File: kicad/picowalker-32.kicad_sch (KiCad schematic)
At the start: 21 parts, among them IC1 TFBS4711-TT1, J1 DBG_HDR, J2 PROGRAM_HDR, SW1 SW_Push, SW2 SW_Push, SW3 SW_Push, U2 M95512-DWDW4TP_K, U3 BMA400, U4 W25Q128JVS

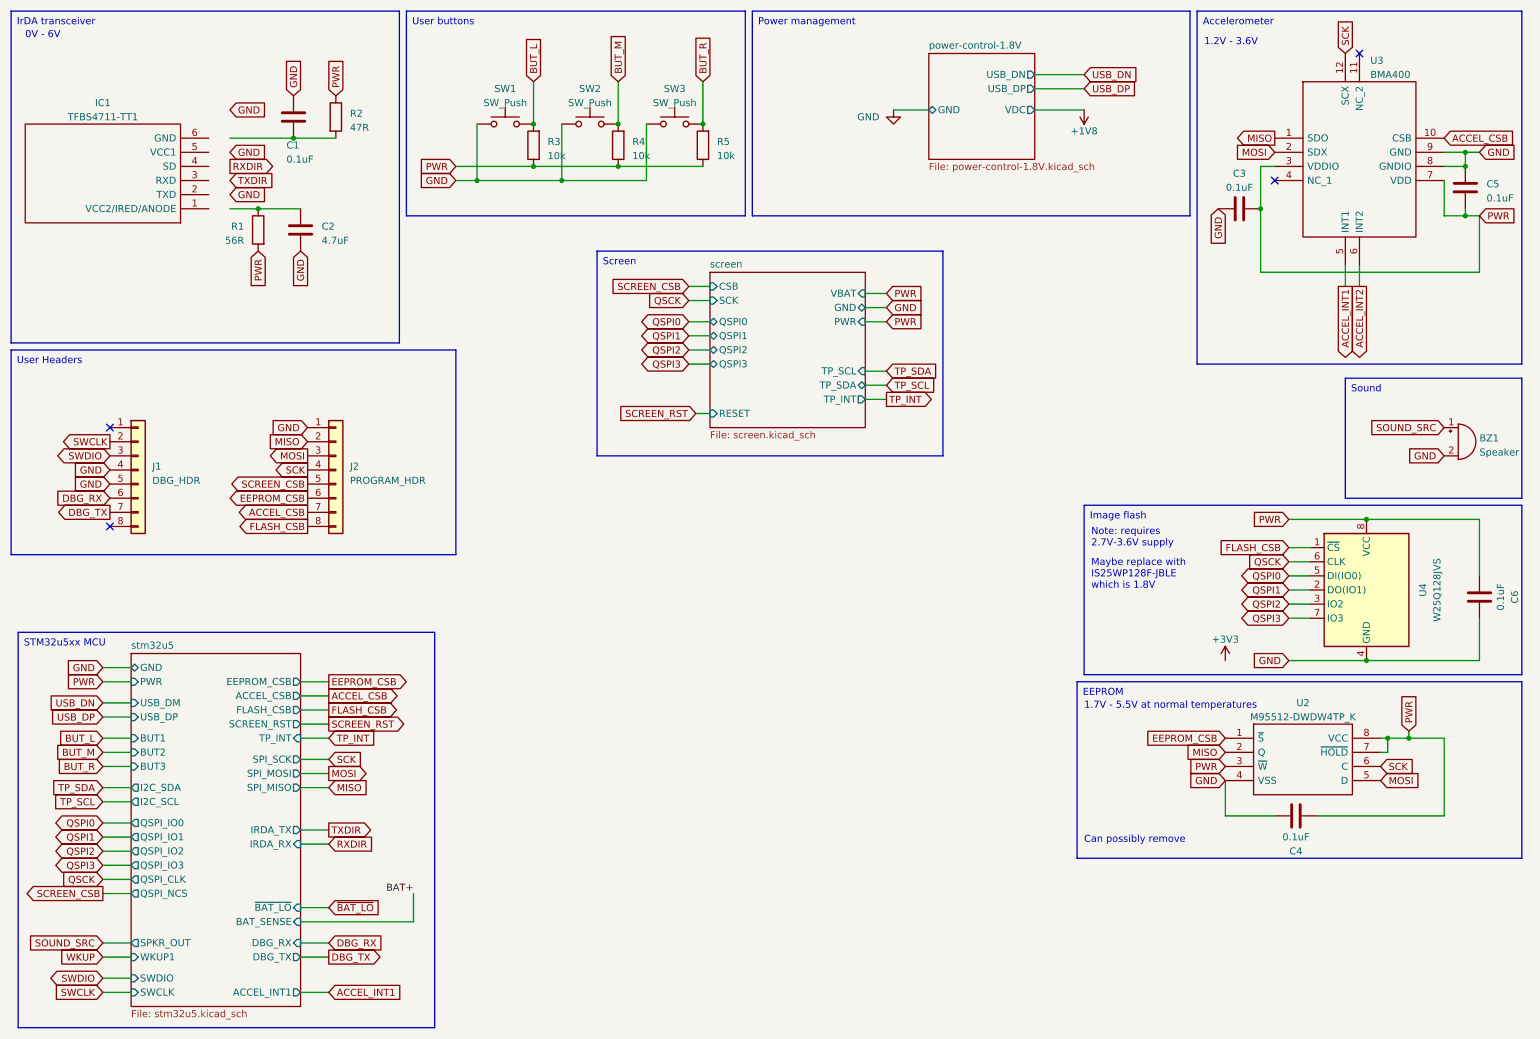
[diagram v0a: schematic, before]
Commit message: Update schematic and add basic PCB layout
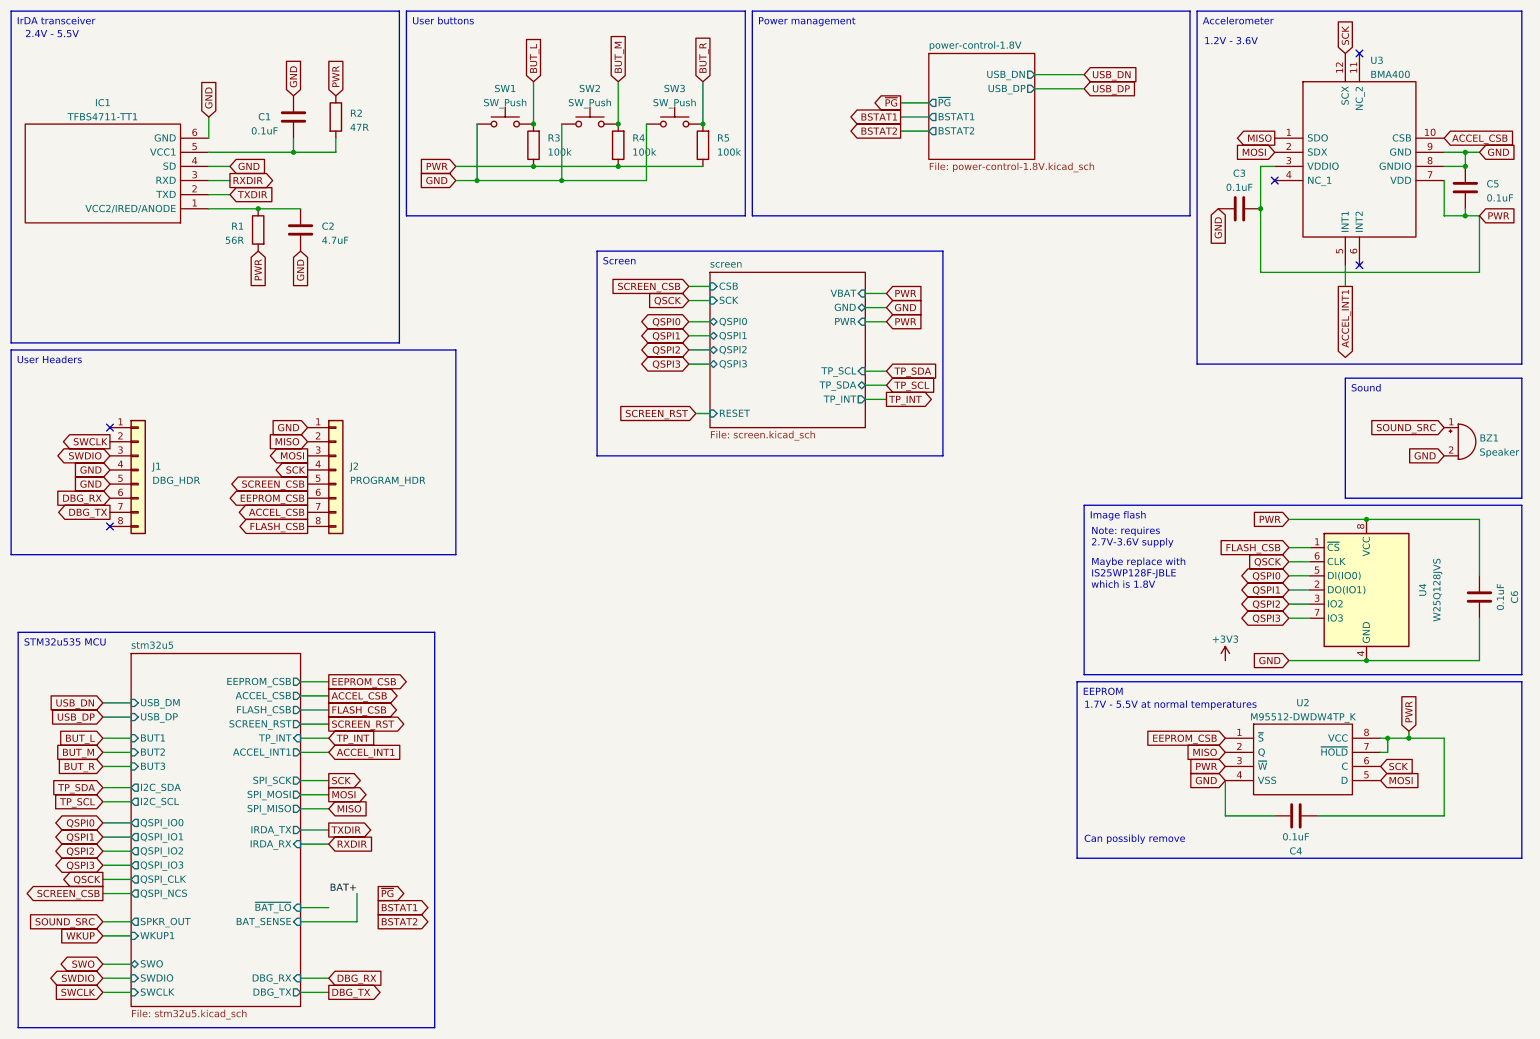
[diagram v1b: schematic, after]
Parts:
- IC1: footprint TFBS4711TT1 -> Samacsys_Parts:TFBS4711TT1
- J1, J2: footprint SamacSys_Parts:SOIC_clipProgSmall -> Samacsys_Parts:SOIC_clipProgSmall
- R3, R4, R5: value 10k -> 100k
- SW1, SW2, SW3: footprint SamacSys_Parts:TL3315NF100Q -> Samacsys_Parts:TL3315NF100Q
- U2: footprint SamacSys_Parts:SOP65P640X120-8N -> Samacsys_Parts:SOP65P640X120-8N
- U3: footprint SamacSys_Parts:BOSCH_LGA-12 -> Samacsys_Parts:BOSCH_LGA-12
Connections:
- net GND: now also IC1.4 (SD), IC1.6 (GND)
- net RXDIR: now also IC1.3 (RXD)
- net TXDIR: now also IC1.2 (TXD)
- net at IC1.1 (VCC2/IRED/ANODE): now also C2.1, R1.1
- net at IC1.5 (VCC1): now also C1.2, R2.2
- net ACCEL_INT2: no longer names the net of U3.6 (INT2)
- no-connect marks 4 -> 5
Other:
- sheet power-control-1.8V ports: added BSTAT1, BSTAT2, ~{PG}; removed GND, VDC
- sheet stm32u5 ports: added SWO; removed GND, PWR
- note added: "2.4V - 5.5V"
- note removed: "0V - 6V"

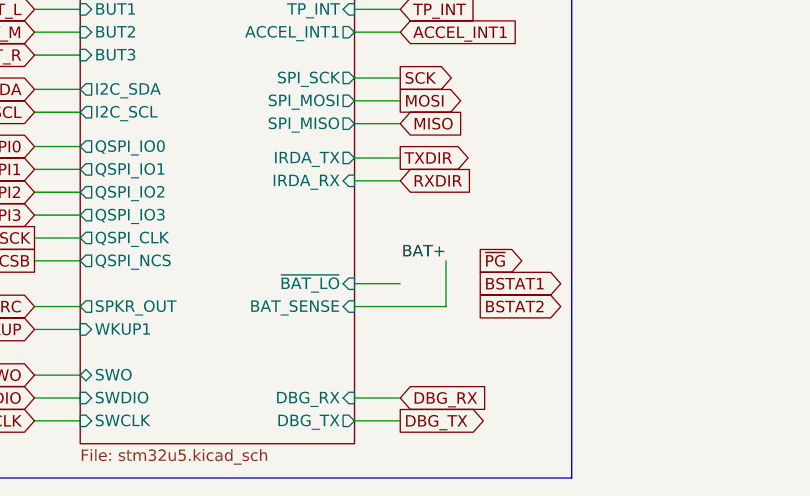
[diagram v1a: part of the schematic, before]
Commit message: Change schematic MCU pinouts
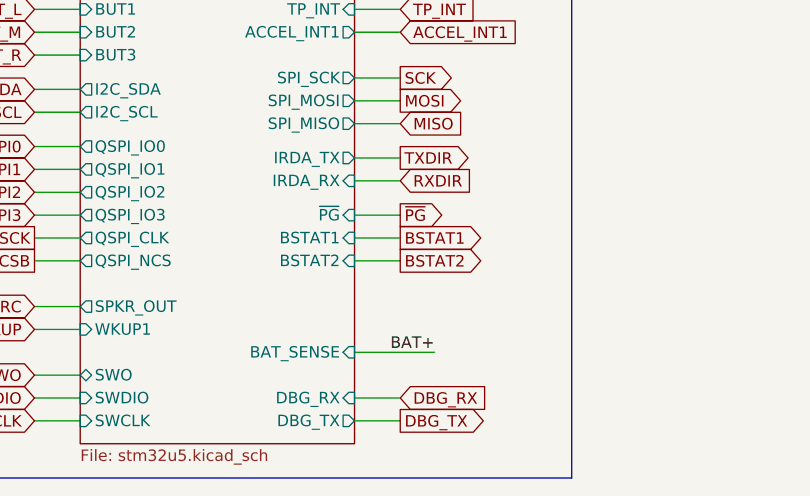
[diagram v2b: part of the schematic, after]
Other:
- sheet stm32u5 ports: added BSTAT1, BSTAT2, ~{PG}; removed ~{BAT_LO}
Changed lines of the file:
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@@
     (stroke (width 0) (type default))
   )
-  (wire (pts (xy 64.77 176.53) (xy 74.93 176.53))
+  (wire (pts (xy 64.77 181.61) (xy 73.66 181.61))
     (stroke (width 0) (type default))
   )
@@
     (stroke (width 0) (type default))
   )
+  (wire (pts (xy 64.77 168.91) (xy 69.85 168.91))
+    (stroke (width 0) (type default))
+  )
   (wire (pts (xy 29.21 176.53) (xy 34.29 176.53))
     (stroke (width 0) (type default))
@@
     (stroke (width 0) (type default))
   )
-  (wire (pts (xy 74.93 176.53) (xy 74.93 171.45))
-    (stroke (width 0) (type default))
-  )
   (wire (pts (xy 237.49 59.69) (xy 237.49 48.26))
     (stroke (width 0) (type default))
@@
     (stroke (width 0) (type default))
   )
-  (wire (pts (xy 64.77 173.99) (xy 69.85 173.99))
-    (stroke (width 0) (type default))
-  )
   (wire (pts (xy 96.52 33.02) (xy 96.52 43.18))
     (stroke (width 0) (type default))
@@
     (stroke (width 0) (type default))
   )
+  (wire (pts (xy 64.77 166.37) (xy 69.85 166.37))
+    (stroke (width 0) (type default))
+  )
   (wire (pts (xy 127 33.02) (xy 127 43.18))
     (stroke (width 0) (type default))
@@
   )
   (wire (pts (xy 166.37 82.55) (xy 170.18 82.55))
+    (stroke (width 0) (type default))
+  )
+  (wire (pts (xy 64.77 171.45) (xy 69.85 171.45))
     (stroke (width 0) (type default))
   )
@@
     (effects (font (size 1.27 1.27)) (justify left bottom))
   )
-  (label "BAT+" (at 74.93 171.45 180) (fields_autoplaced)
+  (label "BAT+" (at 73.66 181.61 180) (fields_autoplaced)
     (effects (font (size 1.27 1.27)) (justify right bottom))
   )
@@
     )
   )
-  (global_label "BSTAT2" (shape output) (at 78.74 176.53 0) (fields_autoplaced)
-    (effects (font (size 1.27 1.27)) (justify left))
-    (property "Intersheetrefs" "${INTERSHEET_REFS}" (at 88.438 176.53 0)
+  (global_label "BSTAT2" (shape output) (at 69.85 171.45 0) (fields_autoplaced)
+    (effects (font (size 1.27 1.27)) (justify left))
+    (property "Intersheetrefs" "${INTERSHEET_REFS}" (at 79.548 171.45 0)
       (effects (font (size 1.27 1.27)) (justify left) hide)
     )
@@
     )
   )
-  (global_label "BSTAT1" (shape output) (at 78.74 173.99 0) (fields_autoplaced)
-    (effects (font (size 1.27 1.27)) (justify left))
-    (property "Intersheetrefs" "${INTERSHEET_REFS}" (at 88.438 173.99 0)
+  (global_label "BSTAT1" (shape output) (at 69.85 168.91 0) (fields_autoplaced)
+    (effects (font (size 1.27 1.27)) (justify left))
+    (property "Intersheetrefs" "${INTERSHEET_REFS}" (at 79.548 168.91 0)
       (effects (font (size 1.27 1.27)) (justify left) hide)
     )
@@
     )
   )
-  (global_label "~{PG}" (shape output) (at 78.74 171.45 0) (fields_autoplaced)
-    (effects (font (size 1.27 1.27)) (justify left))
-    (property "Intersheetrefs" "${INTERSHEET_REFS}" (at 84.2652 171.45 0)
+  (global_label "~{PG}" (shape output) (at 69.85 166.37 0) (fields_autoplaced)
+    (effects (font (size 1.27 1.27)) (justify left))
+    (property "Intersheetrefs" "${INTERSHEET_REFS}" (at 75.3752 166.37 0)
       (effects (font (size 1.27 1.27)) (justify left) hide)
     )
@@
       (effects (font (size 1.27 1.27)) (justify left))
     )
-    (pin "~{BAT_LO}" input (at 64.77 173.99 0)
-      (effects (font (size 1.27 1.27)) (justify right))
-    )
     (pin "I2C_SDA" output (at 34.29 152.4 180)
       (effects (font (size 1.27 1.27)) (justify left))
@@
       (effects (font (size 1.27 1.27)) (justify left))
     )
-    (pin "BAT_SENSE" input (at 64.77 176.53 0)
+    (pin "BAT_SENSE" input (at 64.77 181.61 0)
       (effects (font (size 1.27 1.27)) (justify right))
     )
@@
       (effects (font (size 1.27 1.27)) (justify left))
     )
-    (instances
+    (pin "~{PG}" input (at 64.77 166.37 0)
+      (effects (font (size 1.27 1.27)) (justify right))
+    )
+    (pin "BSTAT1" input (at 64.77 168.91 0)
+      (effects (font (size 1.27 1.27)) (justify right))
+    )
+    (pin "BSTAT2" input (at 64.77 171.45 0)
+      (effects (font (size 1.27 1.27)) (justify right))
+    )
+    (instances

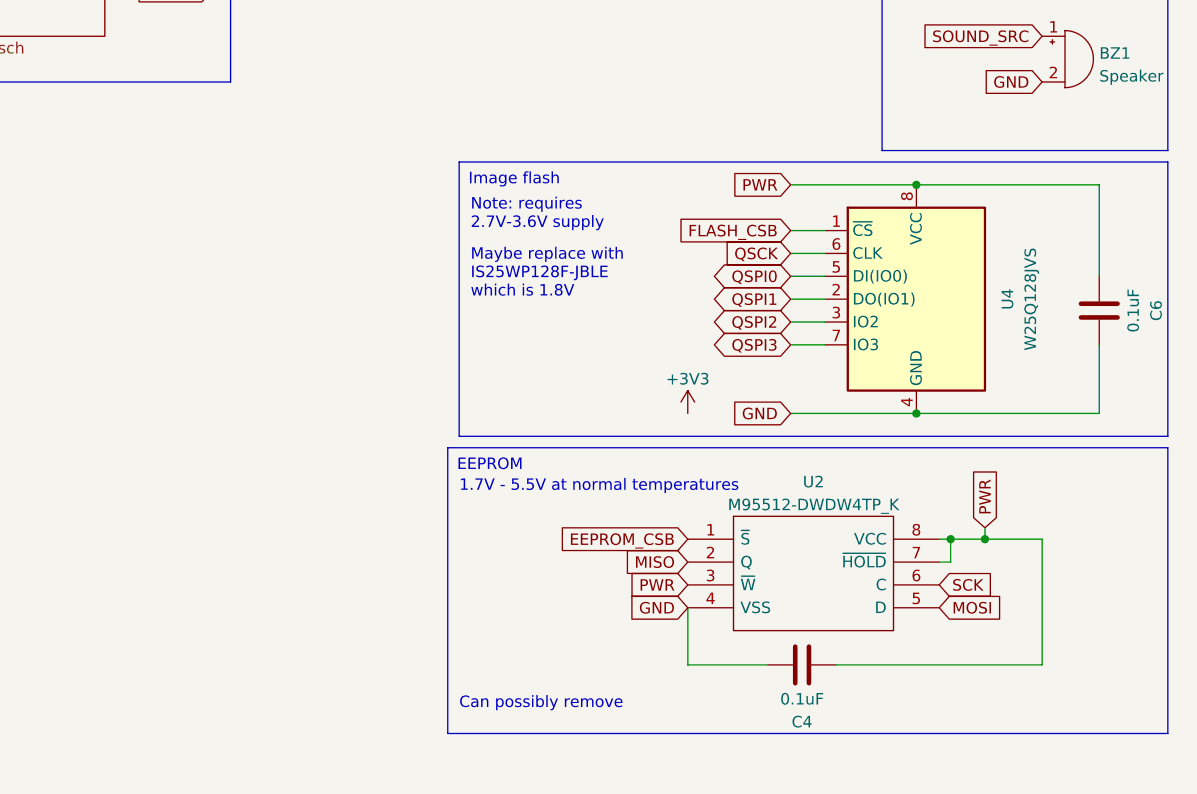
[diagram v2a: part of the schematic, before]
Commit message: comments about power, changed eeprom and flash packages
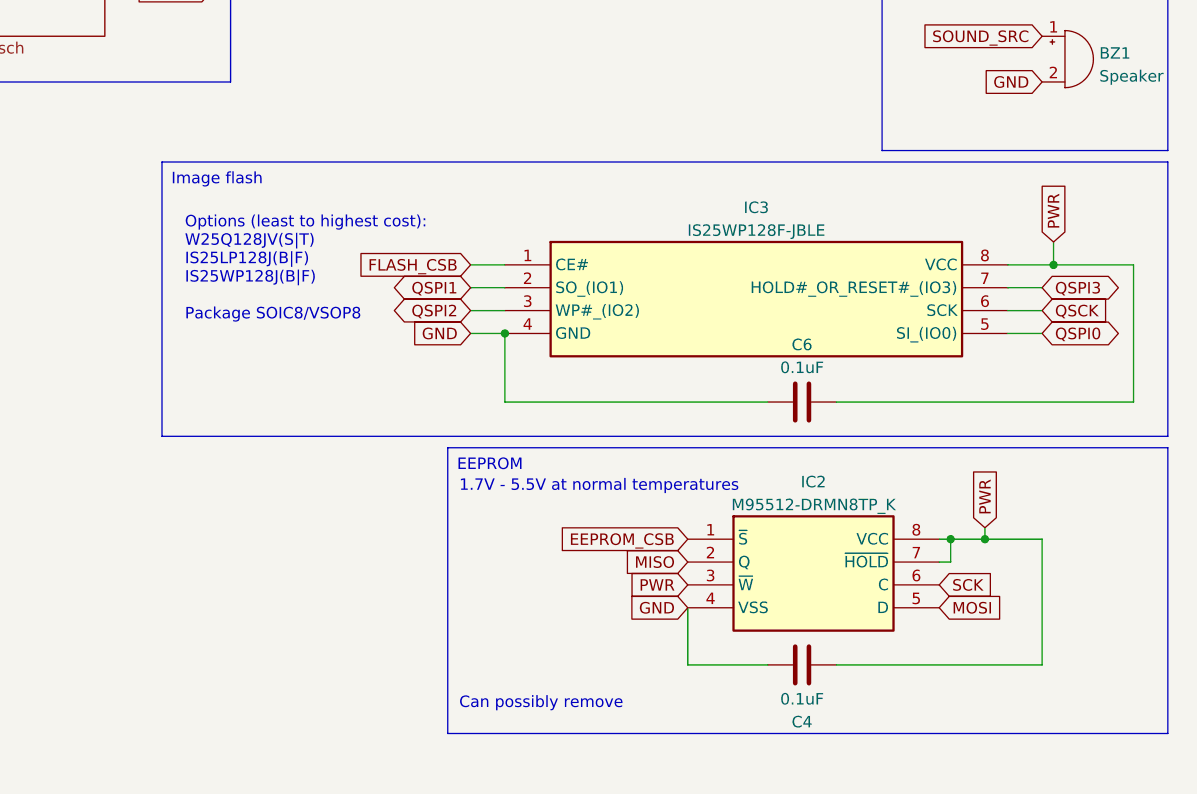
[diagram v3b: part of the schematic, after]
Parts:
- removed U2: M95512-DWDW4TP_K, Samacsys_Parts:SOP65P640X120-8N, symbol SamacSys_Parts:M95512-DWDW4TP_K
- removed U4: W25Q128JVS, Package_SO:SOIC-8_5.23x5.23mm_P1.27mm, symbol Memory_Flash:W25Q128JVS
- added IC2: M95512-DRMN8TP_K, SOIC127P600X175-8N, symbol SamacSys_Parts:M95512-DRMN8TP_K
- added IC3: IS25WP128F-JBLE, SOIC127P790X216-8N, symbol SamacSys_Parts:IS25WP128F-JBLE
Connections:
- net EEPROM_CSB: now also IC2.1 (~{S})
- net FLASH_CSB: now also IC3.1 (CE#)
- net GND: now also C6.1, IC2.4 (VSS), IC3.4 (GND); no longer C6.2
- net MISO: now also IC2.2 (Q)
- net MOSI: now also IC2.5 (D)
- net PWR: now also C6.2, IC2.3 (~{W}), IC2.7 (~{HOLD}), IC2.8 (VCC), IC3.8 (VCC); no longer C6.1
- net QSCK: now also IC3.6 (SCK)
- net QSPI0: now also IC3.5 (SI_(IO0))
- net QSPI1: now also IC3.2 (SO_(IO1))
- net QSPI2: now also IC3.3 (WP#_(IO2))
- net QSPI3: now also IC3.7 (HOLD#_OR_RESET#_(IO3))
- net SCK: now also IC2.6 (C)
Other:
- note added: "Options (least to highest cost): W25Q128JV(S|T) IS25LP128J(B|F) IS25WP128J(B|F) Package SOIC8/VSOP8"
- note removed: "Maybe replace with IS25WP128F-JBLE which is 1.8V"
- note removed: "Note: requires 2.7V-3.6V supply"
- moved on the sheet: C6

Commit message: playing with battery/power circuit
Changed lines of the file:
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@@
     (stroke (width 0) (type default))
   )
-  (wire (pts (xy 64.77 181.61) (xy 73.66 181.61))
+  (wire (pts (xy 64.77 181.61) (xy 77.47 181.61))
     (stroke (width 0) (type default))
   )
@@
     (stroke (width 0) (type default))
   )
-  (wire (pts (xy 166.37 63.5) (xy 170.18 63.5))
+  (wire (pts (xy 166.37 63.5) (xy 177.8 63.5))
     (stroke (width 0) (type default))
   )
@@
     (effects (font (size 1.27 1.27)) (justify left bottom))
   )
-  (label "BAT+" (at 73.66 181.61 180) (fields_autoplaced)
+  (label "PWR_SRC" (at 177.8 63.5 180) (fields_autoplaced)
     (effects (font (size 1.27 1.27)) (justify right bottom))
   )
+  (label "PWR_SRC" (at 77.47 181.61 180) (fields_autoplaced)
+    (effects (font (size 1.27 1.27)) (justify right bottom))
+  )
   (global_label "SOUND_SRC" (shape input) (at 270.51 87.63 180) (fields_autoplaced)
     (effects (font (size 1.27 1.27)) (justify right))
@@
       (effects (font (size 1.27 1.27)) (justify left) hide)
     )
-  )
-  (global_label "PWR" (shape input) (at 170.18 63.5 0) (fields_autoplaced)
-    (effects (font (size 1.27 1.27)) (justify left))
-    (property "Intersheetrefs" "${INTERSHEET_REFS}" (at 177.0772 63.5 0)
-      (effects (font (size 1.27 1.27)) (justify left) hide)
-    )
